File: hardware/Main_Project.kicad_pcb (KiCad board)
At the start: 2 copper layers, 254.1 x 139.2 mm, 80 parts, among them J1 Motors_R, J10 BBBBBBBONUSROUND, J11 Power_Distro, J12 Power_Distro, J13 Power_Distro, J14 Power_Distro, J15 Color_Sensor, J16 Color_Sensor, J17 Magnet, J18 FRDM input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

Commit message: New FRDM Board
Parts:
- removed J6: Motor_Power, TerminalBlock:TerminalBlock_bornier-3_P5.08mm
- added G***: LOGO, LOGO, F.Cu at (119.1, 46.0)
- added J20: Colour_Sensor_0, Connector_Molex:Molex_KK-254_AE-6410-04A_1x04_P2.54mm_Vertical, F.Cu at (56.1, 69.1)
- added J21: Magnet, Connector_Molex:Molex_KK-254_AE-6410-02A_1x02_P2.54mm_Vertical, F.Cu at (56.1, 74.9)
- added J22: FRDM_Power, TerminalBlock:TerminalBlock_bornier-2_P5.08mm, F.Cu at (119.1, 75.4)
- J10: value BBBBBBBONUSROUND -> OLED; footprint Connector_Molex:Molex_KK-254_AE-6410-04A_1x04_P2.54mm_Vertical -> Connector_Molex:Molex_KK-254_AE-6410-08A_1x08_P2.54mm_Vertical
- J8: value Color_Sensor -> Colour_Sensor_1
- J9: value Magnet? -> HC-06_Bluetooth
- moved J8 79.9 mm to (56.1, 107.2)
- moved J9 67.3 mm to (119.1, 58.2)
- moved J7 9.65 mm to (56.1, 58.2)
- moved J10 1.54 mm to (56.1, 96.0)
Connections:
- FRDM1 pad A4: /SDA -> unconnected-(FRDM1-A4/PTC2-PadA4)
- FRDM1 pad A5: /SCL -> unconnected-(FRDM1-A5/PTC1-PadA5)
- FRDM1 pad D0: unconnected-(FRDM1-D0/PTA1-PadD0) -> /L_Enable
- FRDM1 pad D1: /L_Enable -> /R_1
- FRDM1 pad D10: Net-(FRDM1-D10/PTD0) -> /RS
- FRDM1 pad D11: Net-(FRDM1-D11/PTD2) -> /MOSI/Data
- FRDM1 pad D12: Net-(FRDM1-D12/PTD3) -> /MISO
- FRDM1 pad D13: Net-(FRDM1-D13/PTD1) -> /SCK
- FRDM1 pad D14: Net-(FRDM1-SDA/PTE0) -> /SDA_1
- FRDM1 pad D15: Net-(FRDM1-SCL/PTE1) -> /SCL_1
- FRDM1 pad D2: /R_1 -> /R_2
- FRDM1 pad D3: /R_2 -> /R_Enable
- FRDM1 pad D4: /R_Enable -> /L_2
- FRDM1 pad D5: /L_2 -> /L_1
- FRDM1 pad D6: /L_1 -> /SCL_0
- FRDM1 pad D7: unconnected-(FRDM1-D7/PTC9-PadD7) -> /SDA_0
- FRDM1 pad D8: Net-(FRDM1-D8/PTA13) -> /CS
- FRDM1 pad D9: Net-(FRDM1-D9/PTD5) -> /DC
- FRDM1 pad PTE22: unconnected-(FRDM1-PadPTE22) -> /TX
- FRDM1 pad PTE23: unconnected-(FRDM1-PadPTE23) -> /RX
- FRDM1 pad PTE31: unconnected-(FRDM1-PadPTE31) -> Net-(J21-Pin_2)
- J10 pad 1: Net-(FRDM1-SCL/PTE1) -> +3V3
- J10 pad 2: Net-(FRDM1-SDA/PTE0) -> /SCK
- J10 pad 3: Net-(FRDM1-D13/PTD1) -> /MISO
- J10 pad 4: Net-(FRDM1-D12/PTD3) -> /MOSI/Data
- J8 pad 2: /SDA -> /SDA_1
- J8 pad 3: /SCL -> /SCL_1
- J9 pad 1: Net-(FRDM1-D11/PTD2) -> +3V3
- J9 pad 2: Net-(FRDM1-D10/PTD0) -> /TX
- J9 pad 3: Net-(FRDM1-D9/PTD5) -> /RX
- J9 pad 4: Net-(FRDM1-D8/PTA13) -> GND
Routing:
- net +3V3: track 145.4 -> 329.0 mm, vias 0 -> 3
- net Net-(J21-Pin_2): track 0.00 -> 29.6 mm
- net /TX: track 0.00 -> 27.8 mm
- net /RX: track 0.00 -> 22.1 mm
- net /SDA_1: track 0.00 -> 17.3 mm
- net /DC: track 0.00 -> 10.4 mm
- net /SCK: track 0.00 -> 9.85 mm
- net /RS: track 0.00 -> 9.85 mm
- net /MOSI/Data: track 0.00 -> 9.85 mm
- net /MISO: track 0.00 -> 9.85 mm
- net /CS: track 0.00 -> 9.85 mm
- net /SCL_1: track 0.00 -> 9.22 mm
- net /SDA_0: track 0.00 -> 8.69 mm
- net /SCL_0: track 0.00 -> 8.69 mm
- net Net-(FRDM1-SDA/PTE0): track 8.40 -> 0.00 mm
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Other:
- board text removed: "3V3"
- board text removed: "Colour Sensor"
- board text removed: "Extra"
- board text removed: "Motor Driver"

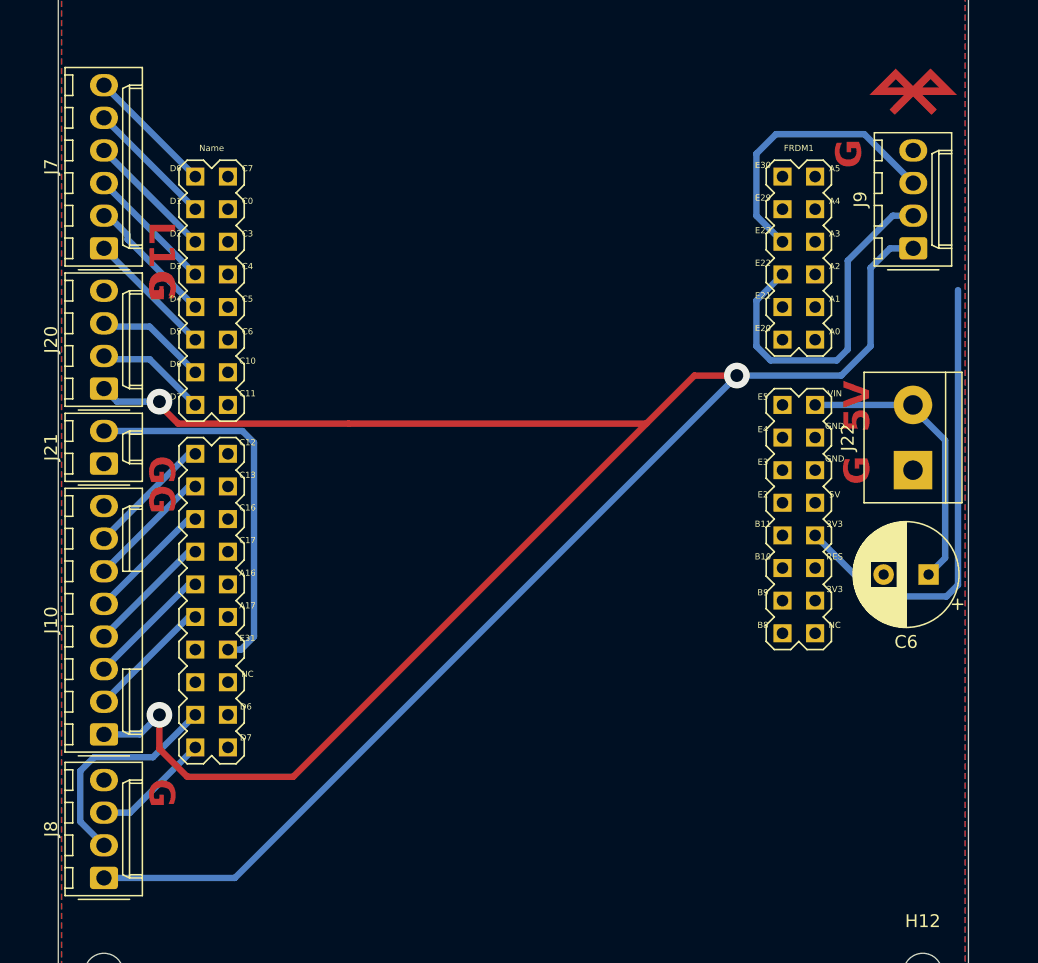
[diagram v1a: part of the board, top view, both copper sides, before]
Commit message: Updated PCB with connections all B-side, and unrouted track fixed
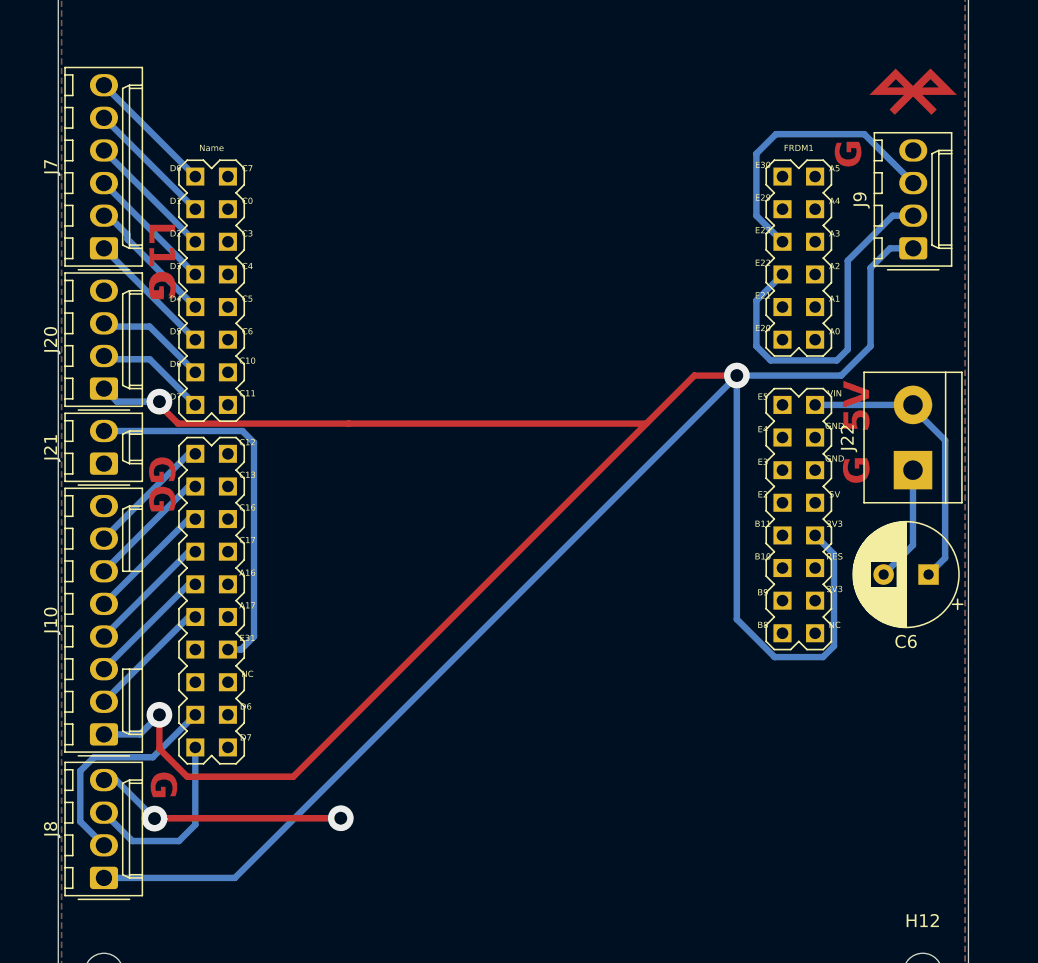
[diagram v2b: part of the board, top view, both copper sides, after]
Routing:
- net GND: track 0.00 -> 28.8 mm, vias 1 -> 3
- net /SCL_1: track 9.22 -> 14.6 mm
- net +3V3: track 329.0 -> 330.2 mm

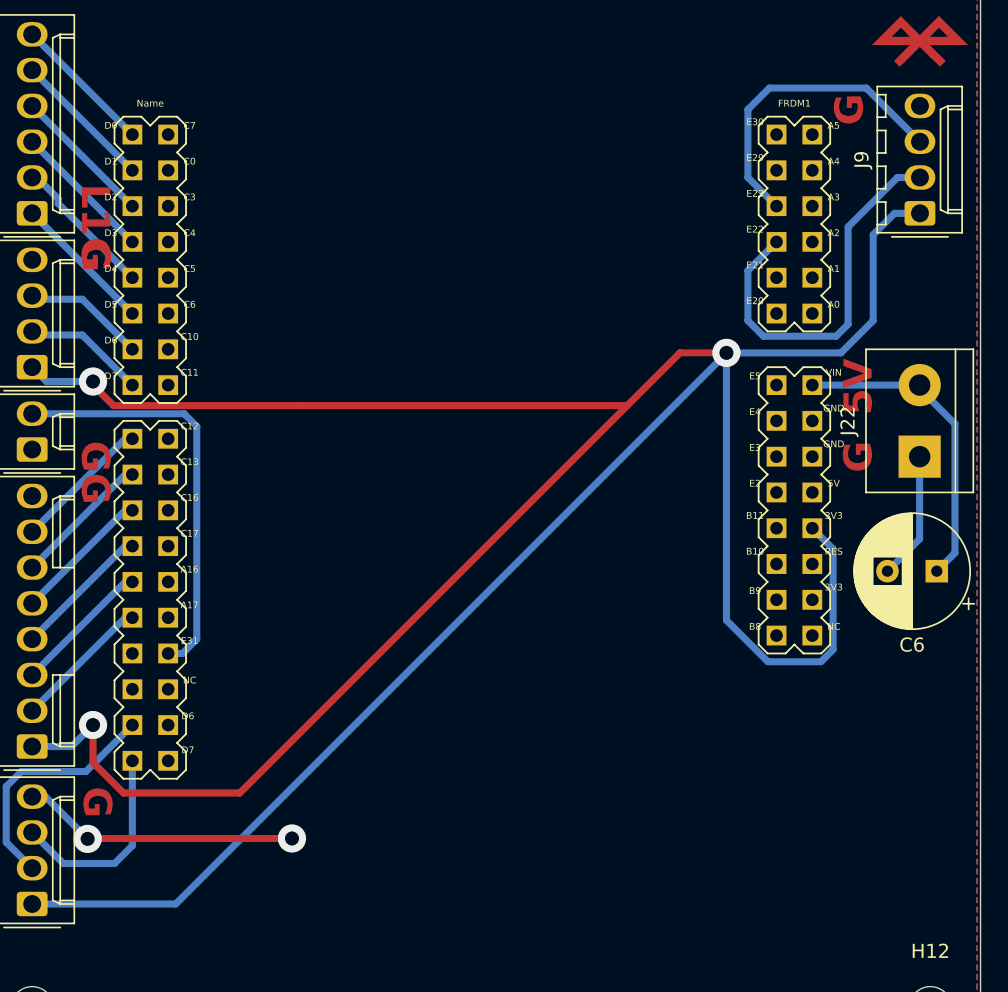
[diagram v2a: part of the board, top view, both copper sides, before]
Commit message: Updated FRDM pcb and photomasks
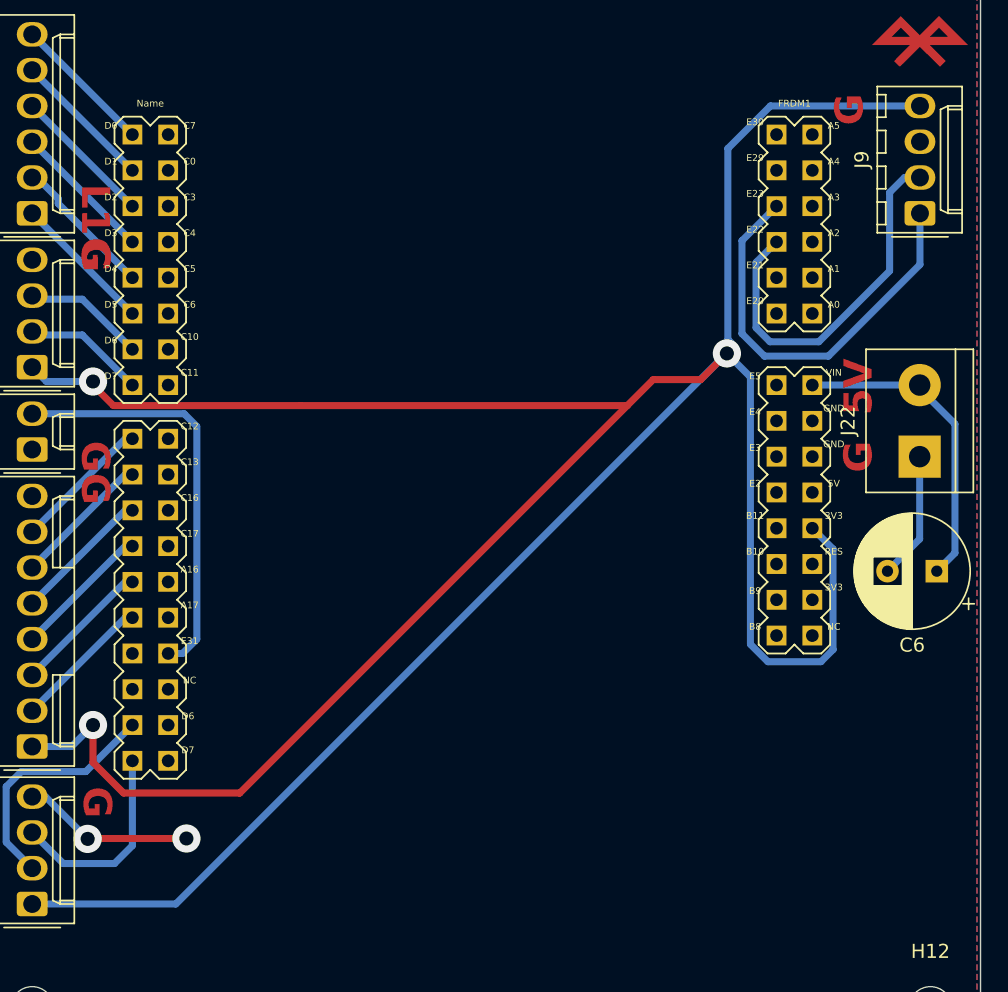
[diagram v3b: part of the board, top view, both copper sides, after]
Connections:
- J9 pad 1: +3V3 -> /RX
- J9 pad 3: /RX -> GND
- J9 pad 4: GND -> +3V3
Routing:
- net +3V3: track 330.2 -> 338.3 mm
- net /RX: track 22.1 -> 30.0 mm
- net GND: track 28.8 -> 21.3 mm
- net /TX: track 27.8 -> 26.8 mm
